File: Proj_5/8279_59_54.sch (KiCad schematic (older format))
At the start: 41 parts, among them J4 Conn_02x07_Counter_Clockwise, J5 Conn_02x07_Counter_Clockwise, SW10 Switch_SW_SPST, SW11 Switch_SW_SPST, SW12 Switch_SW_SPST, SW13 Switch_SW_SPST, SW14 Switch_SW_SPST, SW15 Switch_SW_SPST, SW16 Switch_SW_SPST, SW17 Switch_SW_SPST, SW18 Switch_SW_SPST, SW19 Switch_SW_SPST, SW2 Shift, SW20 Switch_SW_SPST, SW21 Switch_SW_SPST, SW22 Switch_SW_SPST, SW23 Switch_SW_SPST, SW24 NMI Button, SW25 Reset Button, SW26 IR0 Button, SW3 Switch_SW_SPST, SW4 Switch_SW_SPST, SW5 Switch_SW_SPST, SW6 Switch_SW_SPST, SW7 CTRL, SW8 Switch_SW_SPST, SW9 Switch_SW_SPST, U10 8259, U11 8254, U17 pkd8279, U18 74LS138, U48 MAX6816, U49 MAX6816, U50 MAX6816

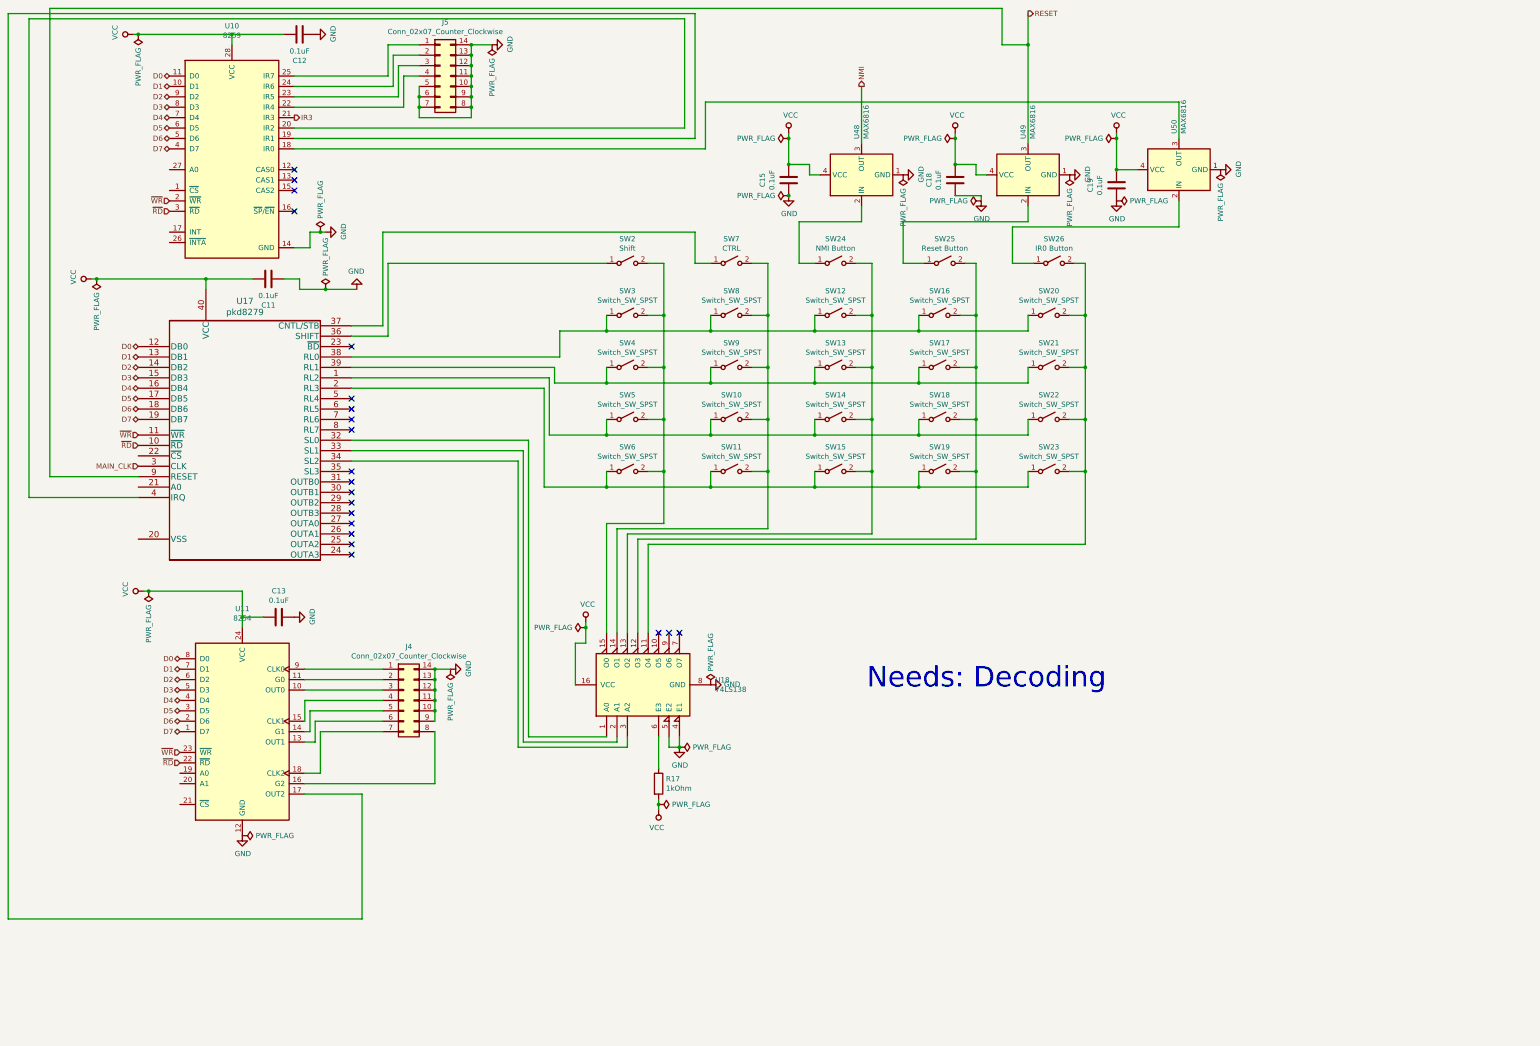
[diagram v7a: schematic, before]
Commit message: Power Flags
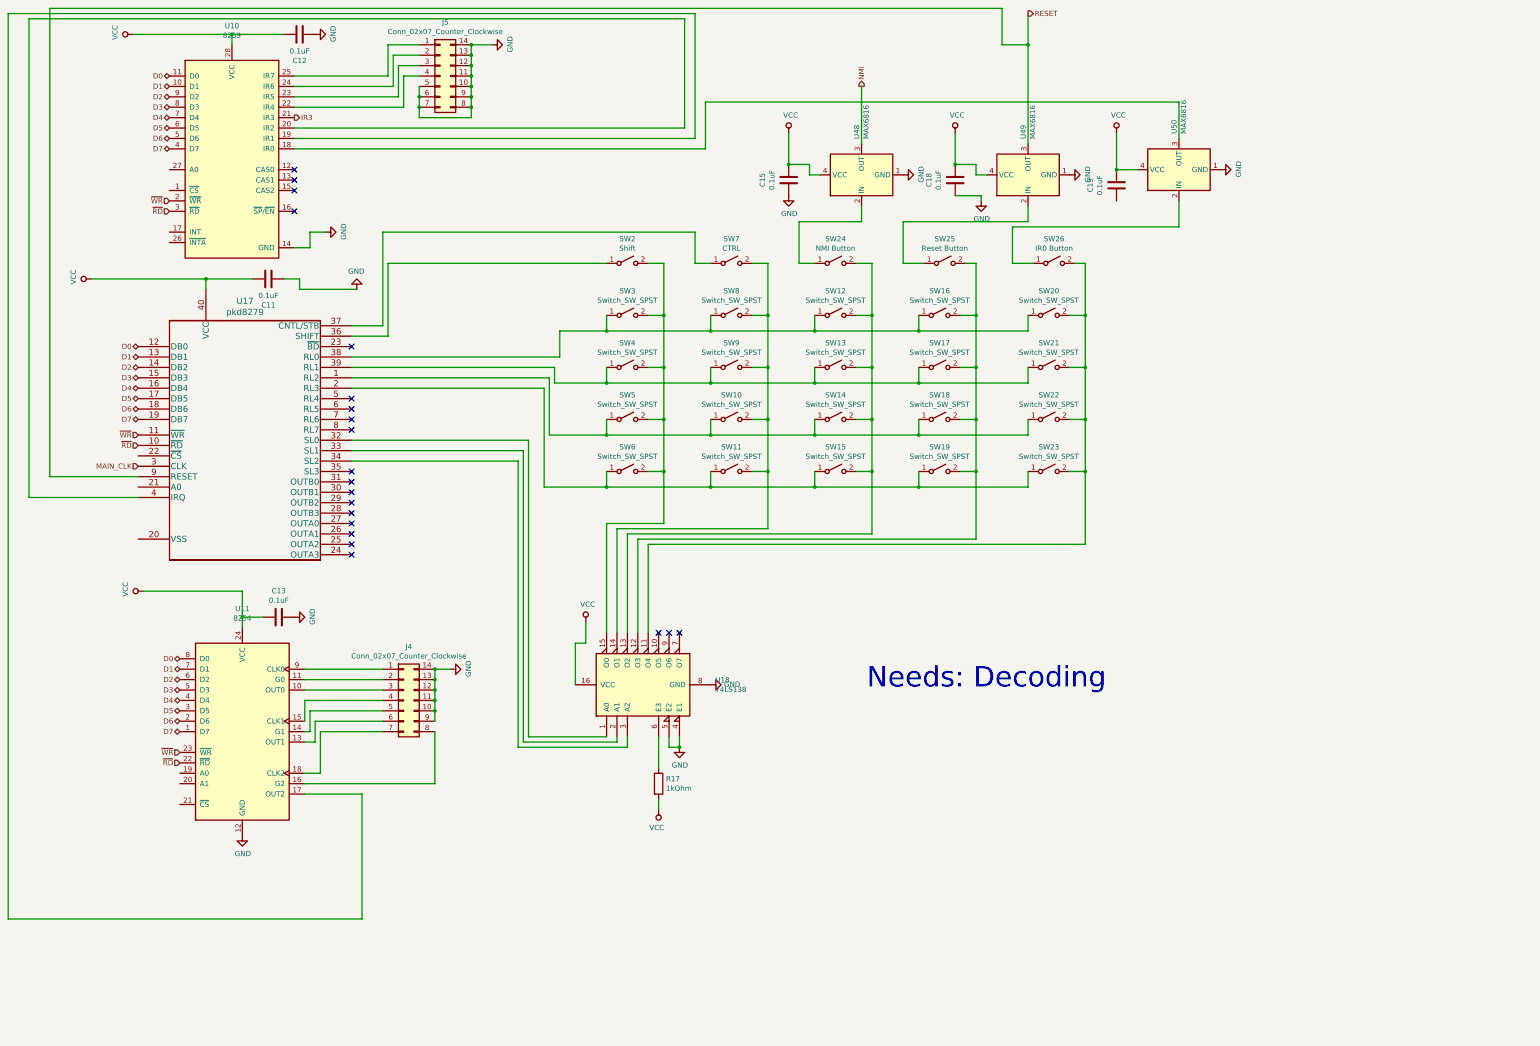
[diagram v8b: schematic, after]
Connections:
- net GND: no longer C19.2
